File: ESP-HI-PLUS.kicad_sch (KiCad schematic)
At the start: 50 parts, among them J1 0.71" LCD, J2 USB_C_Receptacle_USB2.0_14P, J3 Conn_01x09, Q1 NTK3139P, SW1 SW_SPDT, SW2 SW_Push, SW3 SW_Push, U1 ESP32-S3-WROOM-1, U2 DMM-4026-B-I2S-R, U3 MAX98357A, U4 LSM6DSV16X, U5 MAX40200AUK, U6 TLV75733PDBV, U7 TP4065, U8 MAX40200AUK

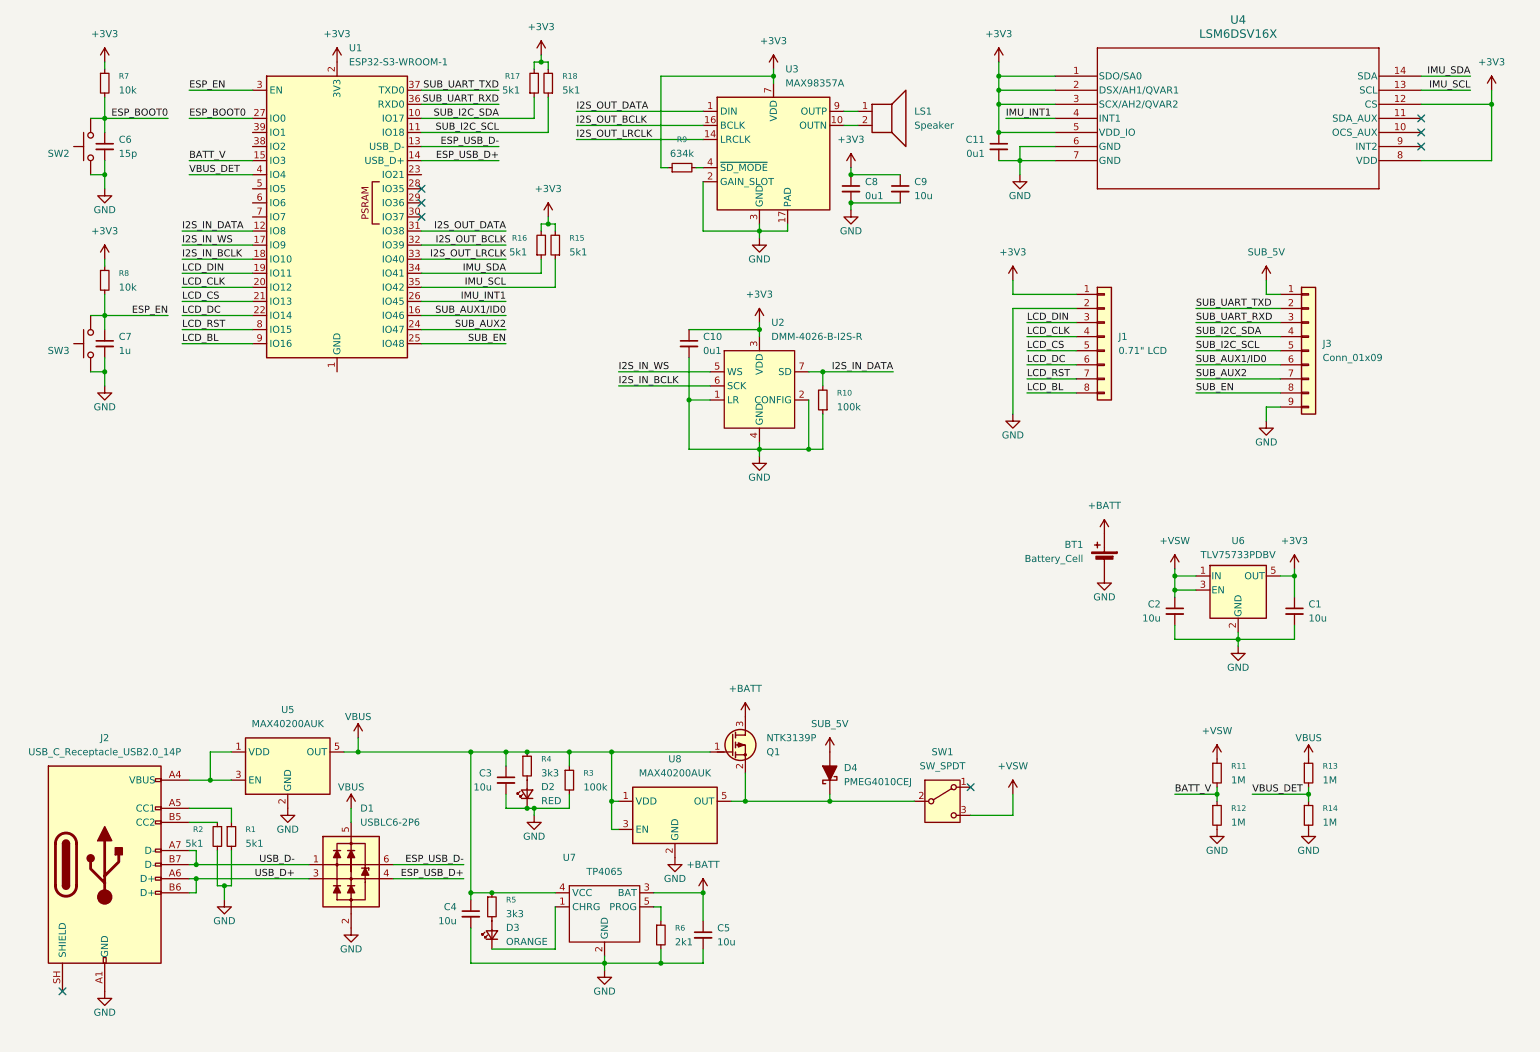
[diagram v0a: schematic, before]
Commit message: update LCD and mounting hole footprints, begin layout
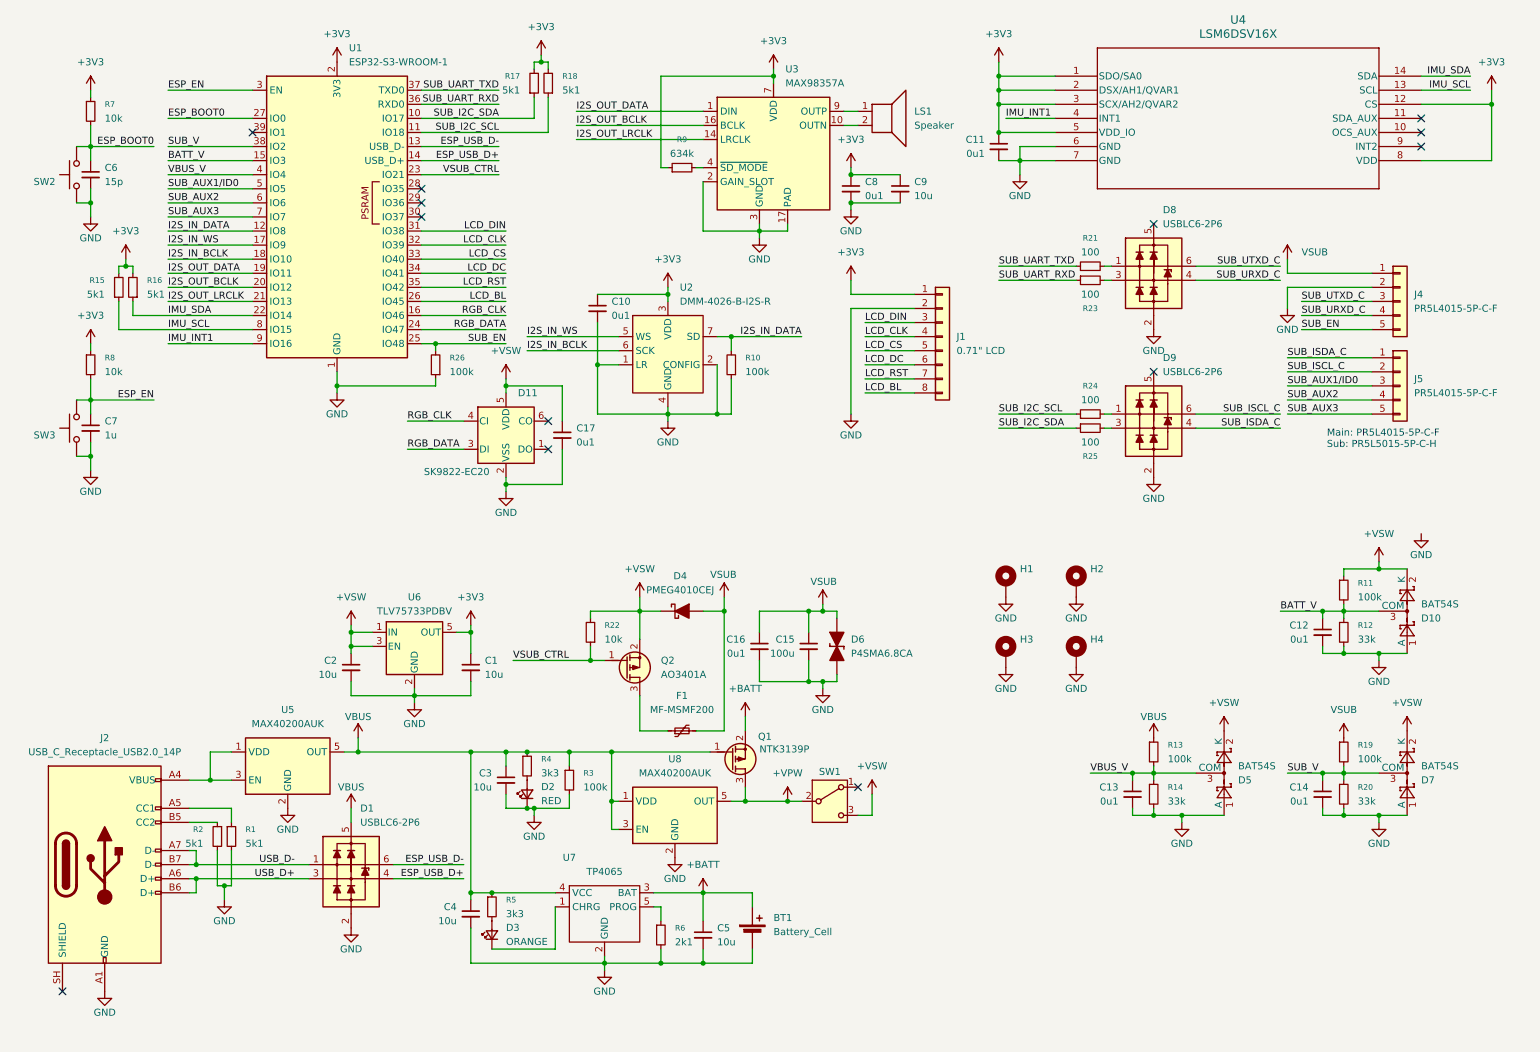
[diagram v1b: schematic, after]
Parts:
- removed J3: Conn_01x09, symbol Connector_Generic:Conn_01x09
- added C12, C13, C14, C16, C17: 0u1, Capacitor_SMD:C_0603_1608Metric, symbol Device:C_Small
- added C15: 100u, Capacitor_SMD:C_1210_3225Metric, symbol Device:C_Small
- added D10, D5, D7: BAT54S, Package_TO_SOT_SMD:SOT-23, symbol Diode:BAT54S
- added D11: SK9822-EC20, PCM_SparkFun-LED:APA102_2020-6Pin, symbol PCM_SparkFun-LED:APA102_2020-6Pin
- added D6: P4SMA6.8CA, PCM_Diode_SMD_AKL:D_SMA_TVS, symbol PCM_Diode_TVS_AKL:P4SMA6.8CA
- added D8, D9: USBLC6-2P6, PCM_Package_TO_SOT_SMD_AKL:SOT-666, symbol PCM_Diode_TVS_AKL:USBLC6-2P6
- added F1: MF-MSMF200, Fuse:Fuse_1812_4532Metric, symbol Device:Polyfuse_Small
- added H1, H2, H3, H4: MountingHole_Pad_MP, MountIngHole_M3_Slim:MountingHole_M3_Slim, symbol Mechanical:MountingHole_Pad_MP
- added J4, J5: PR5L4015-5P-C-F, Connector_PinHeader_2.54mm:PinHeader_1x05_P2.54mm_Vertical, symbol Connector_Generic:Conn_01x05
- added Q2: AO3401A, PCM_Package_TO_SOT_SMD_AKL:SOT-23, symbol PCM_Transistor_MOSFET_AKL:AO3401A
- added R19, R26: 100k, PCM_Resistor_SMD_AKL:R_0603_1608Metric, symbol Device:R_Small
- added R20: 33k, PCM_Resistor_SMD_AKL:R_0603_1608Metric, symbol Device:R_Small
- added R21, R23, R24, R25: 100, PCM_Resistor_SMD_AKL:R_0603_1608Metric, symbol Device:R_Small
- added R22: 10k, PCM_Resistor_SMD_AKL:R_0603_1608Metric, symbol Device:R_Small
- BT1, LS1: footprint (none) -> Connector_Molex:Molex_PicoBlade_53048-0210_1x02_P1.25mm_Horizontal
- D2, D3: footprint (none) -> LED_SMD:LED_0603_1608Metric
- J1: footprint (none) -> Connector_PinSocket_2.54mm:PinSocket_1x08_P2.54mm_Vertical
- J2: footprint (none) -> Connector_USB:USB_C_Receptacle_HCTL_HC-TYPE-C-16P-01A
- R11, R13: value 1M -> 100k
- R12, R14: value 1M -> 33k
- SW1: value SW_SPDT -> MST-12D18G5; footprint (none) -> Button_Switch_SMD:SW_SPDT_CK_JS102011SAQN
- SW2, SW3: value SW_Push -> SKRPACE010; footprint (none) -> Button_Switch_SMD:SW_Push_1P1T_NO_Vertical_Wuerth_434133025816
- U2: footprint (none) -> MIC_DMM-4026-B-I2S-R:MIC_DMM-4026-B-I2S-R
- U4: footprint LGA14_LSM6_STM -> LSM6DSV16X:LGA14_LSM6_STM
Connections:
- net +BATT: now also Q1.2 (S); no longer Q1.3 (D)
- net +VSW: now also D4.1 (K), C17.1, D10.2 (K), D11.5 (VDD), D5.2 (K), D7.2 (K), Q2.2 (S), R22.2
- net BATT_V: now also C12.1, D10.3 (COM)
- net GND: now also U1.1 (GND), U1.40 (GND), U1.41 (GND), C12.2, C13.2, C14.2, C15.2, C16.2, C17.2, D10.1 (A), D11.2 (VSS), D5.1 (A), D6.1 (K), D7.1 (A), D8.2 (VN), D9.2 (VN), H1.MP, H2.MP, H3.MP, H4.MP, J4.2 (Pin_2), R20.2, R26.1
- net I2S_OUT_BCLK: now also U1.20 (IO12); no longer U1.32 (IO39)
- net I2S_OUT_DATA: now also U1.19 (IO11); no longer U1.31 (IO38)
- net I2S_OUT_LRCLK: now also U1.21 (IO13); no longer U1.33 (IO40)
- net IMU_INT1: now also U1.9 (IO16); no longer U1.26 (IO45)
- net IMU_SCL: now also U1.8 (IO15); no longer U1.35 (IO42)
- net IMU_SDA: now also U1.22 (IO14); no longer U1.34 (IO41)
- net LCD_BL: now also U1.26 (IO45); no longer U1.9 (IO16)
- net LCD_CLK: now also U1.32 (IO39); no longer U1.20 (IO12)
- net LCD_CS: now also U1.33 (IO40); no longer U1.21 (IO13)
- net LCD_DC: now also U1.34 (IO41); no longer U1.22 (IO14)
- net LCD_DIN: now also U1.31 (IO38); no longer U1.19 (IO11)
- net LCD_RST: now also U1.35 (IO42); no longer U1.8 (IO15)
- net SUB_AUX1/ID0: now also U1.5 (IO5), J5.3 (Pin_3); no longer U1.16 (IO46)
- net SUB_AUX2: now also U1.6 (IO6), J5.4 (Pin_4); no longer U1.24 (IO47)
- net SUB_EN: now also J4.5 (Pin_5), R26.2
- net SUB_I2C_SCL: now also R24.1
- net SUB_I2C_SDA: now also R25.1
- net SUB_UART_RXD: now also R23.1
- net SUB_UART_TXD: now also R21.1
- net +VPW: now reaches SW1.2 (B), U8.5 (OUT)
- net +VPW: now also Q1.3 (D); no longer D4.1 (K), Q1.2 (S)
- net VSUB_CTRL: now reaches U1.23 (IO21)
- net VSUB_CTRL: now also Q2.1 (G), R22.1
- net SUB_V: now reaches U1.38 (IO2)
- net SUB_V: now also C14.1, D7.3 (COM), R19.2, R20.1
- net SUB_AUX3: now reaches U1.7 (IO7)
- net SUB_AUX3: now also J5.5 (Pin_5)
- net SUB_5V renamed VSUB
- net VSUB: now also C15.1, C16.1, D6.2 (A), F1.2, J4.1 (Pin_1), R19.1
- net VBUS_DET renamed VBUS_V
- net VBUS_V: now also C13.1, D5.3 (COM)
- new net: D8.1 (L1), R21.2
- new net: F1.1, Q2.3 (D)
- new net: D9.1 (L1), R24.2
- new net: D9.3 (L2), R25.2
- new net: D8.3 (L2), R23.2
- new net RGB_CLK: D11.4 (CI), U1.16 (IO46)
- new net RGB_DATA: D11.3 (DI), U1.24 (IO47)
- new net SUB_ISCL_C: D9.6 (L1), J5.2 (Pin_2)
- new net SUB_ISDA_C: D9.4 (L2), J5.1 (Pin_1)
- new net SUB_URXD_C: D8.4 (L2), J4.4 (Pin_4)
- new net SUB_UTXD_C: D8.6 (L1), J4.3 (Pin_3)
- no-connect marks 8 -> 13
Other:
- note added: "Main: PR5L4015-5P-C-F Sub: PR5L5015-5P-C-H"
- moved on the sheet: BT1, C1, C10, C2, C6, C7, J1, Q1, R10, R11, R12, R13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

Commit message: layout completed
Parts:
- removed D6: P4SMA6.8CA, PCM_Diode_SMD_AKL:D_SMA_TVS, symbol PCM_Diode_TVS_AKL:P4SMA6.8CA
- removed R15, R16: 5k1, PCM_Resistor_SMD_AKL:R_0603_1608Metric, symbol Device:R_Small
- added C19: 4n7, Capacitor_SMD:C_0402_1005Metric, symbol Device:C_Small
- added C7: 0u1, Capacitor_SMD:C_0402_1005Metric, symbol Device:C_Small
- added D6: TGL34-6.8CA, PCM_Diode_SMD_AKL:D_SMA_TVS, symbol PCM_Diode_TVS_AKL:TGL34-6.8CA
- added R27: 1M, PCM_Resistor_SMD_AKL:R_0402_1005Metric, symbol Device:R_Small
- added R3, R4: 5k1, PCM_Resistor_SMD_AKL:R_0402_1005Metric, symbol Device:R_Small
- C1: renamed from C6; footprint Capacitor_SMD:C_0603_1608Metric -> Capacitor_SMD:C_0402_1005Metric
- C10: renamed from C5; footprint Capacitor_SMD:C_0603_1608Metric -> Capacitor_SMD:C_0402_1005Metric
- C11: renamed from C16; footprint Capacitor_SMD:C_0603_1608Metric -> Capacitor_SMD:C_0402_1005Metric
- C12: renamed from C15; footprint Capacitor_SMD:C_1210_3225Metric -> Capacitor_SMD:C_0402_1005Metric
- C13: renamed from C8; footprint Capacitor_SMD:C_0603_1608Metric -> Capacitor_SMD:C_0402_1005Metric
- C14: renamed from C9; footprint Capacitor_SMD:C_0603_1608Metric -> Capacitor_SMD:C_0402_1005Metric
- C15: renamed from C11; footprint Capacitor_SMD:C_0603_1608Metric -> Capacitor_SMD:C_0402_1005Metric
- C16: renamed from C13; footprint Capacitor_SMD:C_0603_1608Metric -> Capacitor_SMD:C_0402_1005Metric
- C17: renamed from C12; footprint Capacitor_SMD:C_0603_1608Metric -> Capacitor_SMD:C_0402_1005Metric
- C18: renamed from C14; footprint Capacitor_SMD:C_0603_1608Metric -> Capacitor_SMD:C_0402_1005Metric
- C2: renamed from C7; footprint Capacitor_SMD:C_0603_1608Metric -> Capacitor_SMD:C_0402_1005Metric
- C3: renamed from C2; footprint Capacitor_SMD:C_0603_1608Metric -> Capacitor_SMD:C_0402_1005Metric
- C4: renamed from C1; footprint Capacitor_SMD:C_0603_1608Metric -> Capacitor_SMD:C_0402_1005Metric
- C5: renamed from C4; footprint Capacitor_SMD:C_0603_1608Metric -> Capacitor_SMD:C_0402_1005Metric
- C6: renamed from C3; footprint Capacitor_SMD:C_0603_1608Metric -> Capacitor_SMD:C_0402_1005Metric
- C8: renamed from C17; footprint Capacitor_SMD:C_0603_1608Metric -> Capacitor_SMD:C_0402_1005Metric
- C9: renamed from C10; footprint Capacitor_SMD:C_0603_1608Metric -> Capacitor_SMD:C_0402_1005Metric
- D11: renamed from D7; footprint Package_TO_SOT_SMD:SOT-23 -> PCM_SparkFun-LED:APA102_2020-6Pin
- D3: renamed from D11; footprint PCM_SparkFun-LED:APA102_2020-6Pin -> LED_SMD:LED_0603_1608Metric
- D4: renamed from D2; footprint LED_SMD:LED_0603_1608Metric -> PCM_Diode_SMD_AKL:D_SOD-323F
- D5: renamed from D4; footprint PCM_Diode_SMD_AKL:D_SOD-323F -> Package_TO_SOT_SMD:SOT-23
- D7: renamed from D8; footprint PCM_Package_TO_SOT_SMD_AKL:SOT-666 -> Package_TO_SOT_SMD:SOT-23
- D9: renamed from D5; footprint Package_TO_SOT_SMD:SOT-23 -> PCM_Package_TO_SOT_SMD_AKL:SOT-666
- J1: renamed from J2; footprint Connector_USB:USB_C_Receptacle_HCTL_HC-TYPE-C-16P-01A -> Connector_PinSocket_2.54mm:PinSocket_1x08_P2.54mm_Vertical
- J2: renamed from J1; footprint Connector_PinSocket_2.54mm:PinSocket_1x08_P2.54mm_Vertical -> Connector_USB:USB_C_Receptacle_HCTL_HC-TYPE-C-16P-01A
- Q1: renamed from Q2; footprint PCM_Package_TO_SOT_SMD_AKL:SOT-23 -> PCM_Package_TO_SOT_SMD_AKL:SOT-723
- Q2: renamed from Q1; footprint PCM_Package_TO_SOT_SMD_AKL:SOT-723 -> PCM_Package_TO_SOT_SMD_AKL:SOT-23
- R1: renamed from R7; footprint PCM_Resistor_SMD_AKL:R_0603_1608Metric -> PCM_Resistor_SMD_AKL:R_0402_1005Metric
- R10: renamed from R17; footprint PCM_Resistor_SMD_AKL:R_0603_1608Metric -> PCM_Resistor_SMD_AKL:R_0402_1005Metric
- R11: renamed from R18; footprint PCM_Resistor_SMD_AKL:R_0603_1608Metric -> PCM_Resistor_SMD_AKL:R_0402_1005Metric
- R12: renamed from R3; footprint PCM_Resistor_SMD_AKL:R_0603_1608Metric -> PCM_Resistor_SMD_AKL:R_0402_1005Metric
- R13: renamed from R22; footprint PCM_Resistor_SMD_AKL:R_0603_1608Metric -> PCM_Resistor_SMD_AKL:R_0402_1005Metric
- R14: renamed from R6; footprint PCM_Resistor_SMD_AKL:R_0603_1608Metric -> PCM_Resistor_SMD_AKL:R_0402_1005Metric
- R15: renamed from R9; footprint PCM_Resistor_SMD_AKL:R_0603_1608Metric -> PCM_Resistor_SMD_AKL:R_0402_1005Metric
- R16: renamed from R10; footprint PCM_Resistor_SMD_AKL:R_0603_1608Metric -> PCM_Resistor_SMD_AKL:R_0402_1005Metric
- R17: renamed from R21; footprint PCM_Resistor_SMD_AKL:R_0603_1608Metric -> PCM_Resistor_SMD_AKL:R_0402_1005Metric
- R18: renamed from R23; footprint PCM_Resistor_SMD_AKL:R_0603_1608Metric -> PCM_Resistor_SMD_AKL:R_0402_1005Metric
- R19: renamed from R24; footprint PCM_Resistor_SMD_AKL:R_0603_1608Metric -> PCM_Resistor_SMD_AKL:R_0402_1005Metric
- R2: renamed from R8; footprint PCM_Resistor_SMD_AKL:R_0603_1608Metric -> PCM_Resistor_SMD_AKL:R_0402_1005Metric
- R20: renamed from R25; footprint PCM_Resistor_SMD_AKL:R_0603_1608Metric -> PCM_Resistor_SMD_AKL:R_0402_1005Metric
- R21: renamed from R13; footprint PCM_Resistor_SMD_AKL:R_0603_1608Metric -> PCM_Resistor_SMD_AKL:R_0402_1005Metric
- R22: renamed from R14; footprint PCM_Resistor_SMD_AKL:R_0603_1608Metric -> PCM_Resistor_SMD_AKL:R_0402_1005Metric
- R23: renamed from R11; footprint PCM_Resistor_SMD_AKL:R_0603_1608Metric -> PCM_Resistor_SMD_AKL:R_0402_1005Metric
- R24: renamed from R12; footprint PCM_Resistor_SMD_AKL:R_0603_1608Metric -> PCM_Resistor_SMD_AKL:R_0402_1005Metric
- R25: renamed from R19; footprint PCM_Resistor_SMD_AKL:R_0603_1608Metric -> PCM_Resistor_SMD_AKL:R_0402_1005Metric
- R26: renamed from R20; footprint PCM_Resistor_SMD_AKL:R_0603_1608Metric -> PCM_Resistor_SMD_AKL:R_0402_1005Metric
- R5: renamed from R2; footprint PCM_Resistor_SMD_AKL:R_0603_1608Metric -> PCM_Resistor_SMD_AKL:R_0402_1005Metric
- R6: renamed from R1; footprint PCM_Resistor_SMD_AKL:R_0603_1608Metric -> PCM_Resistor_SMD_AKL:R_0402_1005Metric
- R7: renamed from R26; footprint PCM_Resistor_SMD_AKL:R_0603_1608Metric -> PCM_Resistor_SMD_AKL:R_0402_1005Metric
- R8: renamed from R5; footprint PCM_Resistor_SMD_AKL:R_0603_1608Metric -> PCM_Resistor_SMD_AKL:R_0402_1005Metric
- R9: renamed from R4; footprint PCM_Resistor_SMD_AKL:R_0603_1608Metric -> PCM_Resistor_SMD_AKL:R_0402_1005Metric
- SW1: renamed from SW2; footprint Button_Switch_SMD:SW_Push_1P1T_NO_Vertical_Wuerth_434133025816 -> Button_Switch_SMD:SW_SPDT_CK_JS102011SAQN
- SW3: renamed from SW1; value MST-12D18G5 -> JS102011SAQN; footprint Button_Switch_SMD:SW_SPDT_CK_JS102011SAQN -> Button_Switch_SMD:SW_Push_1P1T_NO_Vertical_Wuerth_434133025816
- U1: renamed from U5; footprint Package_TO_SOT_SMD:SOT-23-5 -> RF_Module:ESP32-S3-WROOM-1
- U2: renamed from U1; footprint RF_Module:ESP32-S3-WROOM-1 -> MIC_DMM-4026-B-I2S-R:MIC_DMM-4026-B-I2S-R
- U3: renamed from U6; footprint Package_TO_SOT_SMD:SOT-23-5 -> Package_DFN_QFN:TQFN-16-1EP_3x3mm_P0.5mm_EP1.23x1.23mm
- U4: renamed from U7; footprint PCM_Package_TO_SOT_SMD_AKL:SOT-23-5_BigPads -> LSM6DSV16X:LGA14_LSM6_STM
- U5: renamed from U2; footprint MIC_DMM-4026-B-I2S-R:MIC_DMM-4026-B-I2S-R -> Package_TO_SOT_SMD:SOT-23-5
- U7: renamed from U3; footprint Package_DFN_QFN:TQFN-16-1EP_3x3mm_P0.5mm_EP1.23x1.23mm -> PCM_Package_TO_SOT_SMD_AKL:SOT-23-5_BigPads
- U8: renamed from U4; footprint LSM6DSV16X:LGA14_LSM6_STM -> Package_TO_SOT_SMD:SOT-23-5
- renumbered D3 to D2, D9 to D8, H3 to H2, H2 to H3, J4 to J3, J5 to J4, SW3 to SW2, U8 to U6
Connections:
- net +3V3: now also C7.1, R3.2, R4.2
- net BATT_V: now also U2.5 (IO5); no longer U2.15 (IO3)
- net GND: now also C19.1, C7.2, D6.1 (K), R27.2; no longer H4.MP
- net I2S_IN_DATA: now also U2.17 (IO9); no longer U2.12 (IO8)
- net I2S_IN_WS: now also U2.19 (IO11); no longer U2.17 (IO9)
- net I2S_OUT_BCLK: now also U2.21 (IO13); no longer U2.20 (IO12)
- net I2S_OUT_DATA: now also U2.20 (IO12); no longer U2.19 (IO11)
- net I2S_OUT_LRCLK: now also U2.22 (IO14); no longer U2.21 (IO13)
- net IMU_INT1: now also U2.7 (IO7); no longer U2.9 (IO16)
- net IMU_SCL: now also U2.9 (IO16), R3.1; no longer U2.8 (IO15)
- net IMU_SDA: now also U2.8 (IO15), R4.1; no longer U2.22 (IO14)
- net LCD_CLK: now also U2.34 (IO41); no longer U2.32 (IO39)
- net LCD_DC: now also U2.32 (IO39); no longer U2.34 (IO41)
- net LCD_DIN: now also U2.35 (IO42); no longer U2.31 (IO38)
- net LCD_RST: now also U2.31 (IO38); no longer U2.35 (IO42)
- net RGB_CLK: now also U2.24 (IO47); no longer U2.16 (IO46)
- net RGB_DATA: now also U2.23 (IO21); no longer U2.24 (IO47)
- net SUB_AUX1/ID0: now also U2.12 (IO8); no longer U2.5 (IO5)
- net SUB_AUX2: now also U2.25 (IO48); no longer U2.6 (IO6)
- net SUB_AUX3: now also U2.38 (IO2); no longer U2.7 (IO7)
- net SUB_EN: now also U2.16 (IO46); no longer U2.25 (IO48)
- net SUB_I2C_SCL: now also R10.1, U2.10 (IO17); no longer R11.1, U2.11 (IO18)
- net SUB_I2C_SDA: now also R11.1, U2.11 (IO18); no longer R10.1, U2.10 (IO17)
- net SUB_UART_RXD: now also R17.1; no longer R18.1
- net SUB_UART_TXD: now also R18.1; no longer R17.1
- net SUB_URXD_C: now also D7.6 (L1), J3.3 (Pin_3); no longer D7.4 (L2), J3.4 (Pin_4)
- net SUB_UTXD_C: now also D7.4 (L2), J3.4 (Pin_4); no longer D7.6 (L1), J3.3 (Pin_3)
- net SUB_V: now also U2.6 (IO6); no longer U2.38 (IO2)
- net VSUB: now also D6.2 (A)
- net VSUB_CTRL: now also U2.15 (IO3); no longer U2.23 (IO21)
- net at U7.10 (OUTN): now also LS1.1; no longer LS1.2
- net at U7.9 (OUTP): now also LS1.2; no longer LS1.1
- net at J1.SH (SHIELD): now also C19.2, R27.1
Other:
- note added: "To Sub-Module"
- moved on the sheet: C2, R2, SW2
